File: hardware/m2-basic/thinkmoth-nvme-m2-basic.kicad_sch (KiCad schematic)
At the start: 21 parts, among them J1 ExpressCard, J2 MDT180M03001, J3 TF-009, U1 GL823K-HCY04

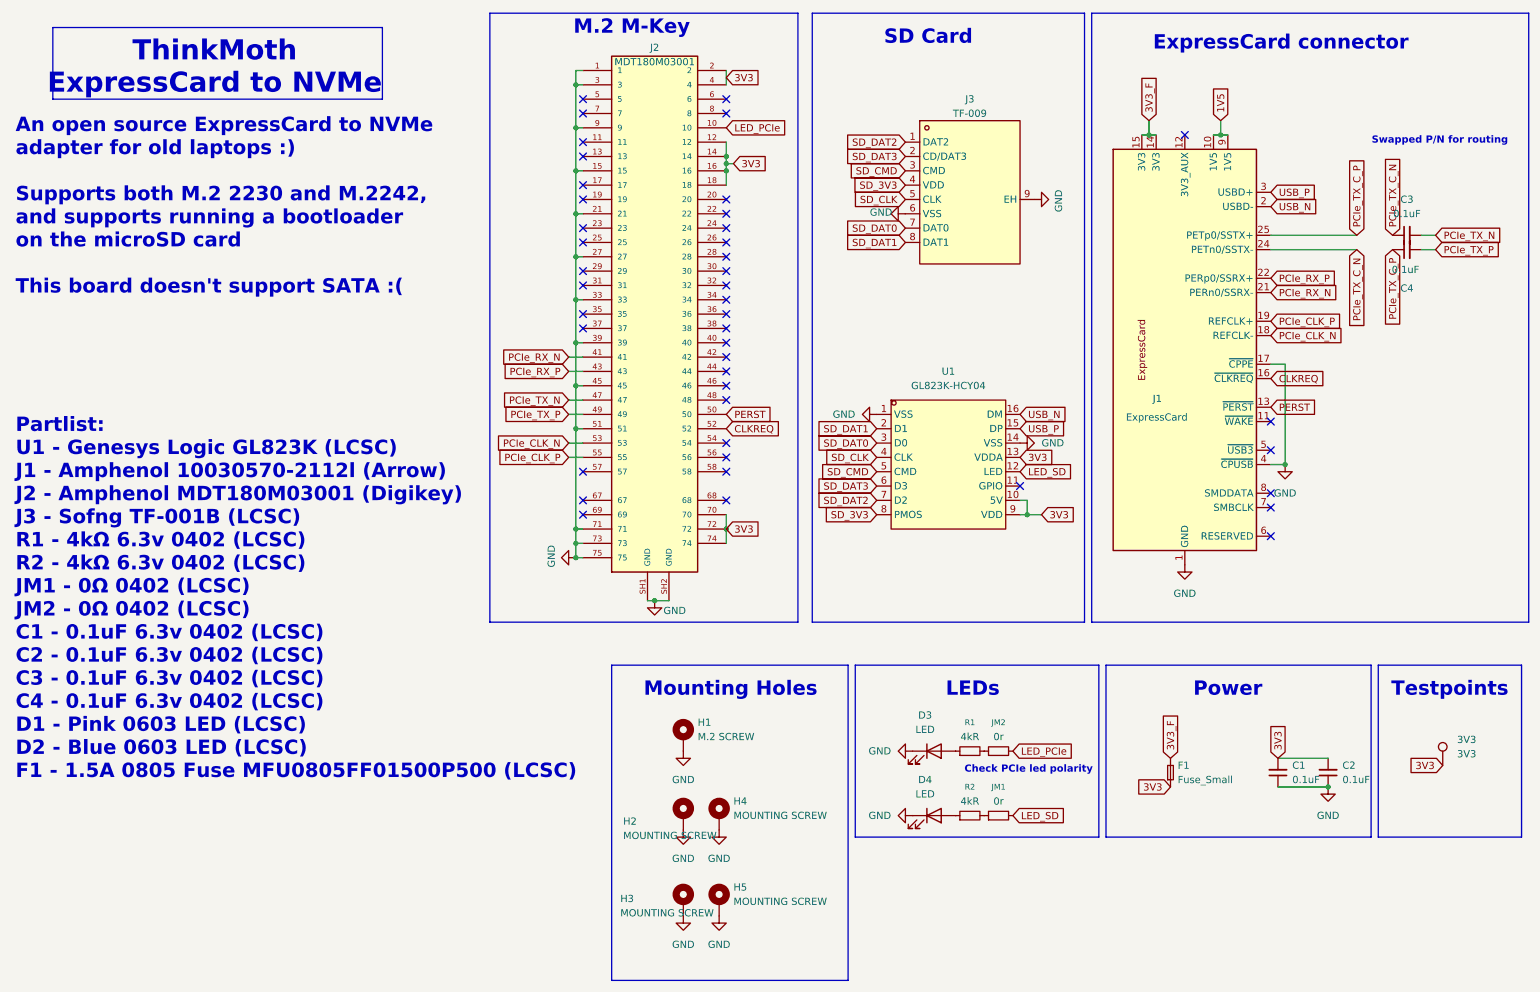
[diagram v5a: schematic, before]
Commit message: Fixed PCIe caps that shouldn't exist, minor routing tweaks
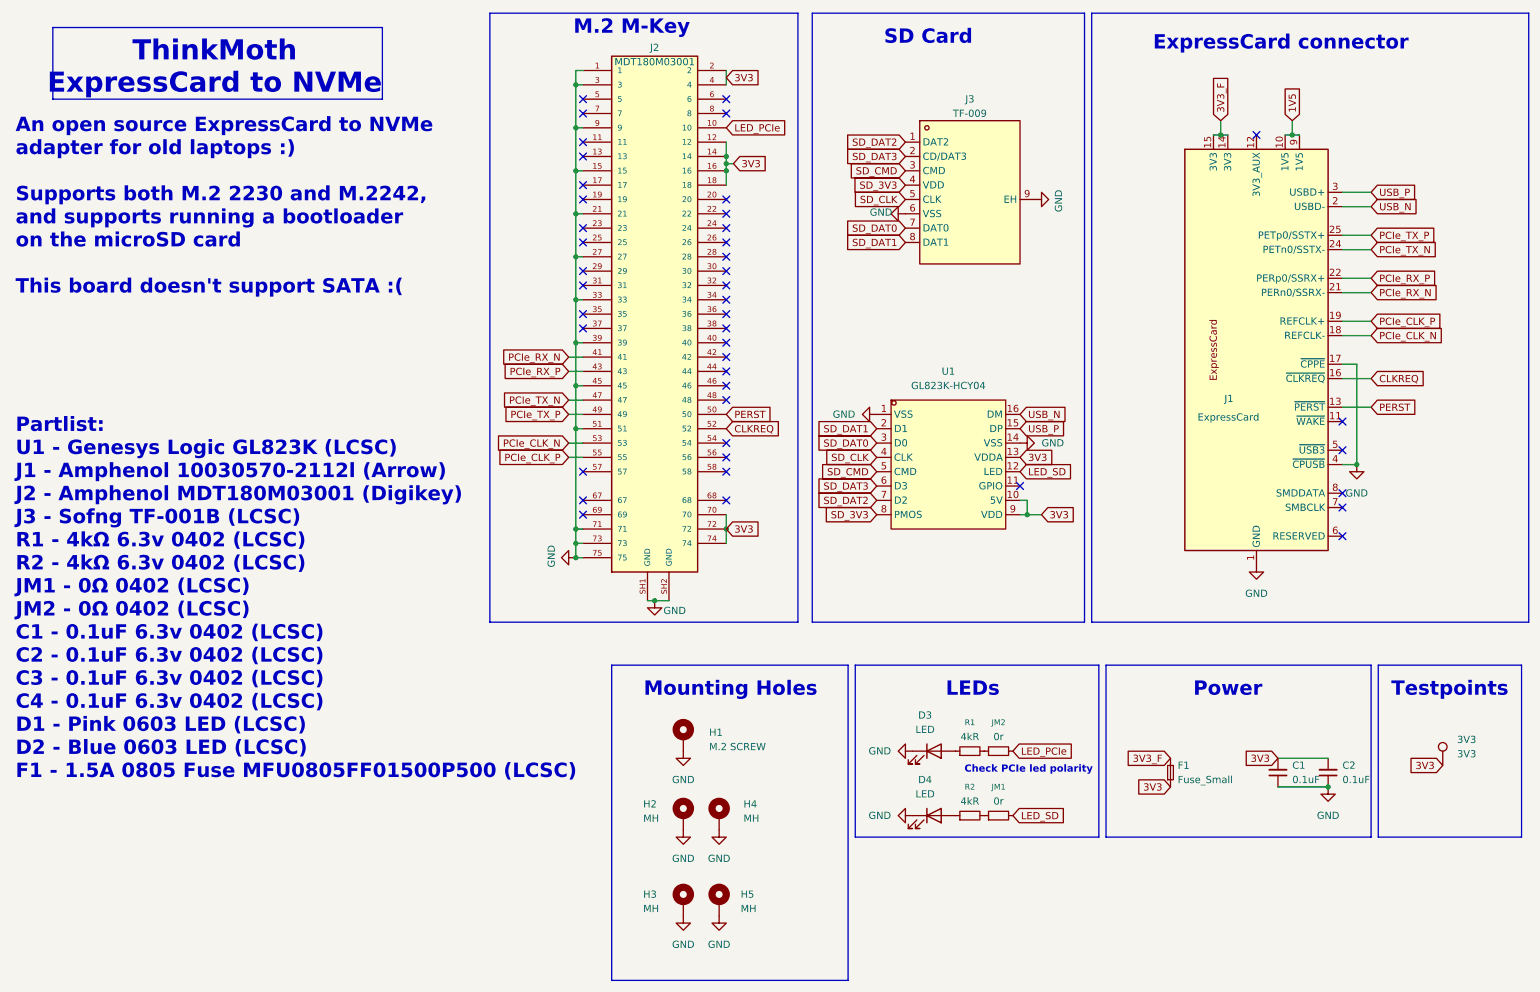
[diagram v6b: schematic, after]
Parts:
- removed C3, C4: 0.1uF, Capacitor_SMD:C_0402_1005Metric, symbol Device:C_Small
- H2, H3, H4, H5: value MOUNTING SCREW -> MH
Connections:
- net PCIe_TX_C_N is gone; now on net PCIe_TX_N: J1.24 (PETn0/SSTX-)
- net PCIe_TX_C_P is gone; now on net PCIe_TX_P: J1.25 (PETp0/SSTX+)
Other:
- note removed: "Swapped P/N for routing"
- moved on the sheet: J1
